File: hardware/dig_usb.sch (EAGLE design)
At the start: 180 parts, among them IC101 AT90USB1287-AU, IC102 74HC166D, IC103 MAX487CSA, IC202 DS1337S, IC301 LTV-356T, IC302 LTV-356T, IC303 LTV-356T, IC304 LTV-356T, IC305 LTV-356T, IC306 LTV-356T, IC307 LTV-356T, IC308 LTV-356T, K401 S202S02, K402 S202S02, K403 S202S02, K404 S202S02, K405 S202S02, K406 S202S02, K407 S202S02, K408 S202S02, Q1 16MHz, Q201 32,768kHz, T301 BCR191, T302 BCR191, T303 BCR191, T304 BCR191, T305 BCR191, T306 BCR191, T307 BCR191, T308 BCR191, X1 AKL_249-08, X102 ISP, X2 AKL_249-08, X3 AKL_230-02, X301 RIA-73-02, X302 RIA-73-02, X303 RIA-73-02, X304 RIA-73-02, X305 RIA-73-02, X4 AKL_230-02, X401 RIA-73-02, X402 RIA-73-02, X403 RIA-73-02, X404 RIA-73-02, X405 RIA-73-02, X406 RIA-73-02, X407 RIA-73-02, X5 AKL_230-04

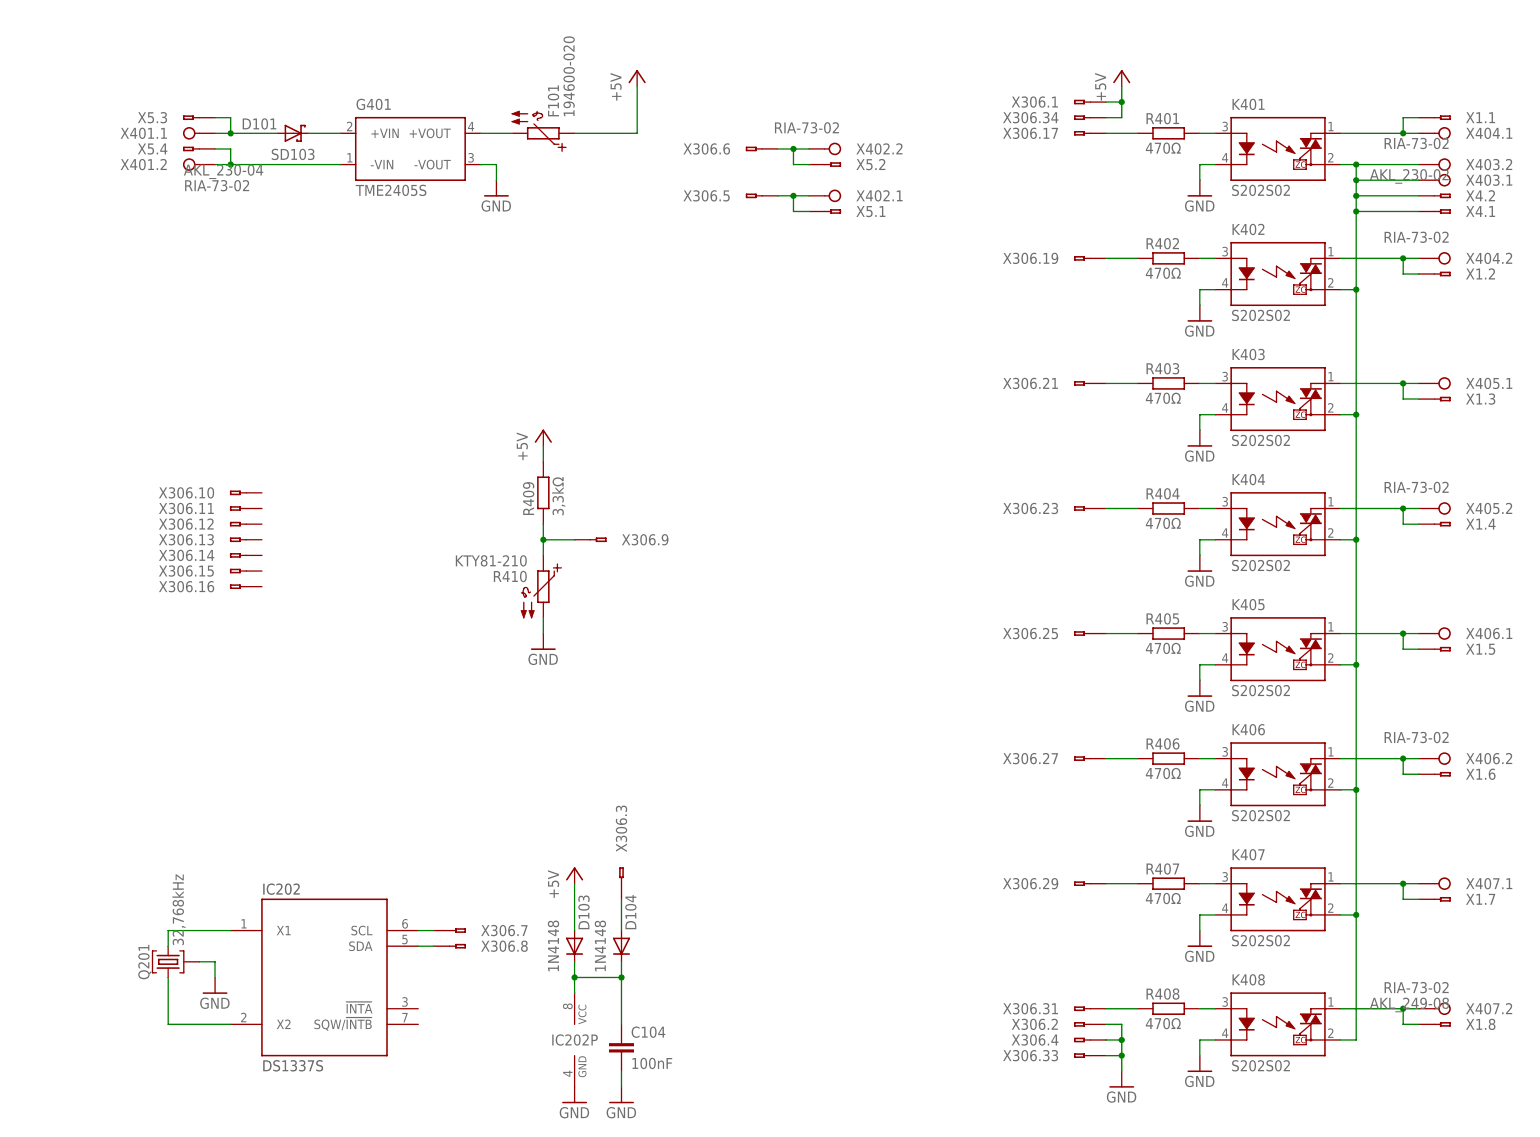
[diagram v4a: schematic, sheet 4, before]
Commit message: RJ45 Buchsen für Bus an dig_usb
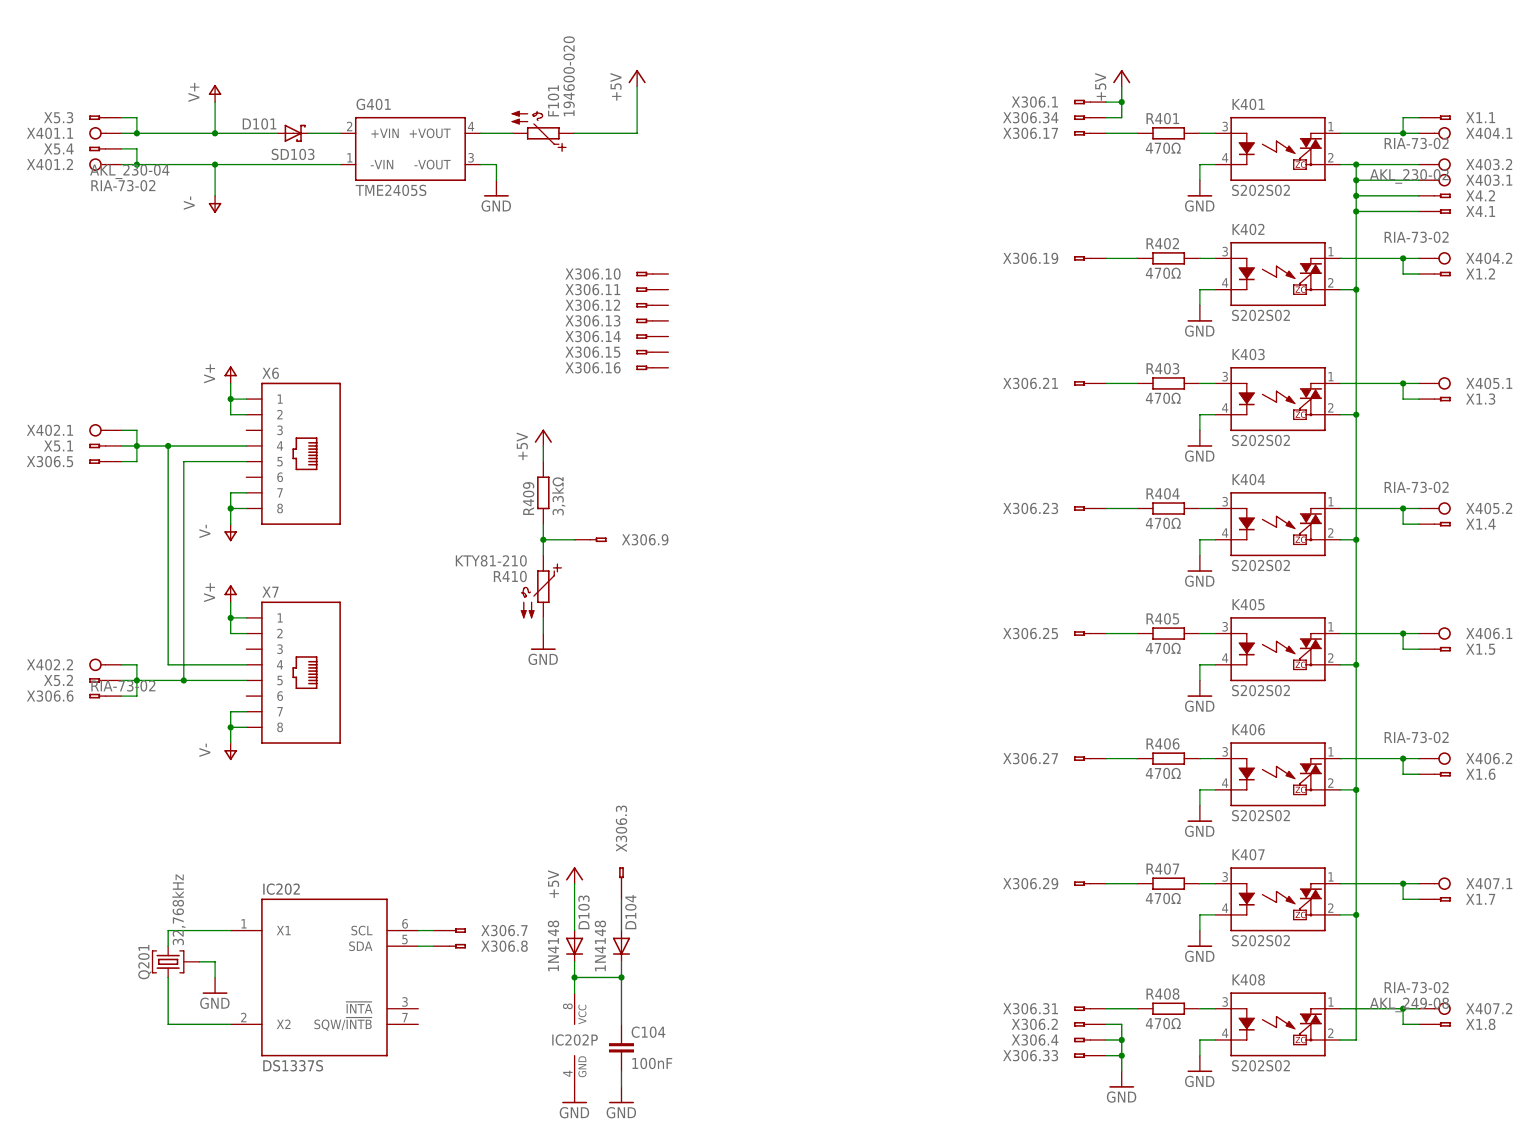
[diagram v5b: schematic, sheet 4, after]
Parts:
- added X6, X7: (no value), stecker:8P8C
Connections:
- removed net N$19: G401.-VIN, X401.2.A, X5.4.A
- removed net N$24: D101.A, X401.1.A, X5.3.A
- new net V+: D101.A, X401.1.A, X5.3.A, X6.1, X6.2, X7.1, X7.2
- new net V-: G401.-VIN, X401.2.A, X5.4.A, X6.7, X6.8, X7.7, X7.8
- net N$133: now also X6.5, X7.5
- net N$134: now also X6.4, X7.4
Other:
- moved on the sheet: X306.10, X306.11, X306.12, X306.13, X306.14, X306.15, X306.16, X306.5, X306.6, X401.1, X401.2, X402.1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

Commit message: dig_usb: Bauteile neu nummeriert und Plan etwas verschönert
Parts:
- removed C1, C2, C3, C4, C5, C6, C7, C8: 1μF, passiv:C_1206
- removed C11: 100nF, passiv:C_0805
- removed C201, C202: 100nF, passiv:C_0603
- removed D1, D11, D13, D15, D3, D5, D7, D9: 91V, diode:Z-DIODE-SOD123
- removed D10, D12, D14, D16, D2, D4, D6, D8: (no value), diode:DIODE-DO214AC
- removed D103, D104: 1N4148, diode:DIODE-SOD123
- removed D17, D18, D19, D20, D21, D22, D23, D24, D25, D26, D27, D28: GN, led:LED_0805
- removed D33: MMSZ5222BT1, diode:Z-DIODE-SOD123
- removed Q201: 32,768kHz, passiv:QM_MS1V-T1K
- removed R12, R13, R14, R15, R16, R17, R18, R19, R20, R21, R22, R23, R24, R3, R6, R9: 47kΩ, passiv:R_1206
- removed R25, R26, R27, R28, R33, R34, R35, R36, R37, R38, R39, R40: 1,5kΩ, passiv:R_0805
- removed R30: 22Ω, passiv:R_0805
- removed S2: (no value), schalter:JUMPER
- removed T301, T302, T303, T304, T305, T306, T307, T308: BCR191, transistor:PNP2R-SOT23-BEC
- removed X1, X2: AKL_249-08, anschluss:AKL_249-08
- removed X3: AKL_230-02, anschluss:AKL_230-02
- removed X5: AKL_230-04, anschluss:AKL_230-04
- removed X6, X7: (no value), stecker:8P8C
- added C110, C111, C401: 100nF, passiv:C_0603
- added C301, C302, C303, C304, C305, C306, C307, C308: 1μF, passiv:C_1206
- added D301, D303, D305, D307, D309, D311, D313, D315: MRA4007, diode:DIODE-DO214AC
- added D302, D304, D306, D308, D310, D312, D314, D316: 91V, diode:Z-DIODE-SOD123
- added D401: SD103, diode:SHOTKY-DIODE-SOD123
- added D402, D403: 1N4148, diode:DIODE-SOD123
- added LED201, LED202, LED203, LED204, LED205, LED206, LED207, LED208, LED209, LED210, LED211, LED212: GN, led:LED_0805
- added Q301, Q302, Q303, Q304, Q305, Q306, Q307, Q308: BCR191, transistor:PNP2R-SOT23-BEC
- added Q401: 32,768kHz, passiv:QM_MS1V-T1K
- added R103: 10k, passiv:R_0805
- added R106: 1MΩ, passiv:R_0805
- added R107, R108: 22kΩ, widerstandsnetzwerk:EXB-38V
- added R112: 120Ω, passiv:R_0805
- added R202, R203, R204, R205, R206, R210, R211, R212: 1,5kΩ, passiv:R_0805
- added R303, R304, R305, R306, R309, R310, R311, R312, R315, R316, R317, R318, R321, R322, R323, R324: 47kΩ, passiv:R_1206
- added S103: (no value), schalter:DP08D
- added X307, X408, X410, X411, X412: RIA-73-02, anschluss:RIA-73-02
- added X308: AKL_249-08, anschluss:AKL_249-08
- C102: device passiv:C_0603 -> passiv:C_0805
- D101: value SD103 -> MMSZ5222BT1; device diode:SHOTKY-DIODE-SOD123 -> diode:Z-DIODE-SOD123
- IC102: value 74HC166D -> MAX487CSA; device ic-logik:74HC166D -> ic-wandler:MAX487CSA
- IC103: value MAX487CSA -> 74HC166D; device ic-wandler:MAX487CSA -> ic-logik:74HC166D
- R102: value 1MΩ -> 22Ω
- R201: value 10k -> 1,5kΩ
- R207: value 120Ω -> 1,5kΩ
- R208, R209: value 22kΩ -> 1,5kΩ; device widerstandsnetzwerk:EXB-38V -> passiv:R_0805
- R401: value 470Ω -> 3,3kΩ
- R402: value 470Ω -> KTY81-210; device passiv:R_0805 -> sensor:KTY81-210
- R409: value 3,3kΩ -> 470Ω
- R410: value KTY81-210 -> 470Ω; device sensor:KTY81-210 -> passiv:R_0805
- S101: device schalter:DP08D -> schalter:JUMPER
- X301: value RIA-73-02 -> AKL_230-02; device anschluss:RIA-73-02 -> anschluss:AKL_230-02
- X303: value RIA-73-02 -> (none); device anschluss:RIA-73-02 -> anschluss:WS34V
- X306: value (none) -> RIA-73-02; device anschluss:WS34V -> anschluss:RIA-73-02
- X403: value RIA-73-02 -> AKL_230-04; device anschluss:RIA-73-02 -> anschluss:AKL_230-04
- X404, X405: value RIA-73-02 -> (none); device anschluss:RIA-73-02 -> stecker:8P8C
- X406: value RIA-73-02 -> AKL_249-08; device anschluss:RIA-73-02 -> anschluss:AKL_249-08
- renumbered C10 to C106, C12 to C103, C13 to C108, C204 to C105, C205 to C107, C9 to C109, D102 to LED104, D201 to LED101, D202 to LED102, D203 to LED103, D29 to LED213, D30 to LED214, D31 to LED215, D32 to LED216, F101 to F401, G401 to V401, IC202 to IC401, Q1 to Q101, R1 to R302, R10 to R320, R11 to R319, R2 to R301, R29 to R110, R31 to R101, R32 to R105, R4 to R308, R41 to R213, R42 to R214, R43 to R215, R44 to R216, R45 to R109, R46 to R111, R47 to R113, R48 to R104, R5 to R307, R7 to R314, R8 to R313, S1 to S102, X4 to X409
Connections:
- net !R: now also IC103A.!CLR; no longer IC102A.!CLR
- net !RESET: now also R103.1; no longer R201.1
- net +5V: now also C104.1, C110.1, C111.1, D402.A, Q301.E, Q302.E, Q303.E, Q304.E, Q305.E, Q306.E, Q307.E, Q308.E, R103.2, R401.2, S101.P$1, S103A.3, S103B.3, S103C.3, S103D.3, S103E.3, S103F.3, S103G.3, X303.1.A, X303.34.A; no longer C102.1, C201.1, C202.1, D103.A, R201.2, R409.2, S101A.3, S101B.3, S101C.3, S101D.3, S101E.3, S101F.3, S101G.3, S2.P$1, T301.E, T302.E, T303.E, T304.E, T305.E, T306.E, T307.E, T308.E, X306.1.A, X306.34.A
- net C1: now also IC103A.CK; no longer IC102A.CK
- net C2: now also IC103A.SH/!LD; no longer IC102A.SH/!LD
- net DI: now also IC103A.QH; no longer IC102A.QH
- net GND: now also C110.2, C111.2, C401.2, D101.A, IC103A.CKI, IC103A.H, IC103A.SI, Q401.G, R107.1, R107.3, R107.5, R107.7, R108.1, R108.3, R108.5, R108.7, R201.1, R202.1, R203.1, R204.1, R205.1, R206.1, R207.1, R210.1, R211.1, R212.1, R402.2, X303.2.A, X303.33.A, X303.4.A; no longer C11.2, C201.2, C202.2, D33.A, IC102A.CKI, IC102A.H, IC102A.SI, Q201.G, R208.3, R208.5, R208.7, R209.3, R209.5, R209.7, R25.1, R26.1, R27.1, R28.1, R33.1, R34.1, R35.1, R36.1, R37.1, R38.1, R39.1, R40.1, R410.2, X306.2.A, X306.33.A, X306.4.A
- net GNDIO: now also C301.2, C302.2, C303.2, C304.2, C305.2, C306.2, C307.2, C308.2, D302.A, D304.A, D306.A, D308.A, D310.A, D312.A, D314.A, D316.A, X302.1.A, X302.2.A; no longer C1.2, C2.2, C3.2, C4.2, C5.2, C6.2, C7.2, C8.2, D1.A, D11.A, D13.A, D15.A, D3.A, D5.A, D7.A, D9.A, X3.1.A, X3.2.A
- net IN0: now also LED201.A; no longer D17.A
- net IN1: now also LED202.A; no longer D18.A
- net IN2: now also LED203.A; no longer D19.A
- net IN3: now also LED204.A; no longer D20.A
- net IN4: now also LED205.A; no longer D21.A
- net IN5: now also LED206.A; no longer D22.A
- net IN6: now also LED207.A; no longer D23.A
- net IN7: now also LED208.A; no longer D24.A
- net L: now also X408.1.A, X408.2.A; no longer X403.1.A, X403.2.A
- net N$10: now also D309.A; no longer D6.A
- net N$100: now also Q306.C, X303.30.A; no longer T307.C, X306.30.A
- net N$101: now also Q308.C, X303.32.A; no longer T308.C, X306.32.A
- net N$102: now also LED201.C, R201.2; no longer D17.C, R25.2
- net N$103: now also LED202.C, R202.2; no longer D18.C, R33.2
- net N$104: now also LED203.C, R203.2; no longer D19.C, R34.2
- net N$105: now also LED204.C, R204.2; no longer D20.C, R35.2
- net N$106: now also LED205.C, R205.2; no longer D21.C, R26.2
- net N$107: now also LED206.C, R206.2; no longer D22.C, R27.2
- net N$108: now also LED207.C, R207.2; no longer D23.C, R28.2
- net N$109: now also LED208.C, R208.2; no longer D24.C, R36.2
- net N$11: now also C305.1, D309.K, D310.K, R317.2; no longer C3.1, D5.K, D6.K, R9.2
- net N$110: now also LED209.C, R209.2; no longer D25.C, R37.2
- net N$111: now also LED210.C, R210.2; no longer D26.C, R38.2
- net N$112: now also LED211.C, R211.2; no longer D27.C, R39.2
- net N$113: now also LED212.C, R212.2; no longer D28.C, R40.2
- net N$119: now also R102.1; no longer R30.1
- net N$120: now also R102.2; no longer R30.2
- net N$124: now also S101.P$2; no longer S2.P$2
- net N$126: now also Q401.2; no longer Q201.2
- net N$127: now also Q401.1; no longer Q201.1
- net N$129: now also D101.K; no longer D33.K
- net N$13: now also IC305.A, R317.1; no longer IC303.A, R9.1
- net N$130: now also D403.A, X303.3.A; no longer D104.A, X306.3.A
- net N$131: now also X303.7.A; no longer X306.7.A
- net N$132: now also X303.8.A; no longer X306.8.A
- net N$133: now also X303.6.A, X403.2.A, X404.5, X405.5; no longer X306.6.A, X5.2.A, X6.5, X7.5
- net N$134: now also X303.5.A, X403.1.A, X404.4, X405.4; no longer X306.5.A, X5.1.A, X6.4, X7.4
- net N$14: now also D313.A; no longer D8.A
- net N$143: now also R106.1; no longer R102.1
- net N$146: now also R401.1, R402.1, X303.9.A; no longer R409.1, R410.1, X306.9.A
- net N$15: now also C307.1, D313.K, D314.K, R323.2; no longer C4.1, D7.K, D8.K, R12.2
- net N$16: now also R404.2; no longer R402.2
- net N$2: now also D301.A; no longer D2.A
- net N$20: now also IC102A.A, S103H.4; no longer IC103A.A, S101H.4
- net N$21: now also R106.2; no longer R102.2
- net N$22: now also IC102A.B, R112.1; no longer IC103A.B, R207.1
- net N$23: now also D401.K; no longer D101.K
- net N$25: now also R405.2; no longer R403.2
- net N$26: now also IC103A.A, R107.2, S103A.4; no longer IC102A.A, R208.2, S101A.4
- net N$27: now also IC103A.B, R107.4, S103B.4; no longer IC102A.B, R208.4, S101B.4
- net N$28: now also IC103A.C, R107.6, S103C.4; no longer IC102A.C, R208.6, S101C.4
- net N$29: now also IC103A.D, R107.8, S103D.4; no longer IC102A.D, R208.8, S101D.4
- net N$3: now also C301.1, D301.K, D302.K, R305.2; no longer C1.1, D1.K, D2.K, R3.2
- net N$30: now also IC103A.E, R108.2, S103E.4; no longer IC102A.E, R209.2, S101E.4
- net N$31: now also IC103A.F, R108.4, S103F.4; no longer IC102A.F, R209.4, S101F.4
- net N$32: now also IC103A.G, R108.6, S103G.4; no longer IC102A.G, R209.6, S101G.4
- net N$33: now also R112.2, S103H.3; no longer R207.2, S101H.3
- net N$34: now also IC307.A, R323.1; no longer IC304.A, R12.1
- net N$35: now also D303.A, R304.1; no longer D10.A, R13.1
- net N$36: now also C302.1, D303.K, D304.K, R306.2; no longer C5.1, D10.K, D9.K, R15.2
- net N$37: now also R406.2; no longer R404.2
- net N$38: now also IC302.A, R306.1; no longer IC305.A, R15.1
- net N$39: now also D307.A, R310.1; no longer D12.A, R16.1
- net N$40: now also C304.1, D307.K, D308.K, R312.2; no longer C6.1, D11.K, D12.K, R18.2
- net N$42: now also R407.2; no longer R405.2
- net N$45: now also X304.1.A, X308.7.A; no longer X2.7.A, X302.1.A
- net N$46: now also X304.2.A, X308.8.A; no longer X2.8.A, X302.2.A
- net N$47: now also X306.1.A, X308.5.A; no longer X2.5.A, X303.1.A
- net N$48: now also X306.2.A, X308.6.A; no longer X2.6.A, X303.2.A
- net N$49: now also R303.1, R304.2; no longer R13.2, R14.1
- net N$5: now also R305.1; no longer R3.1
- net N$50: now also R408.2; no longer R406.2
- net N$51: now also R309.1, R310.2; no longer R16.2, R17.1
- net N$52: now also IC307.C, Q307.B; no longer IC304.C, T304.B
- net N$53: now also R315.1, R316.2; no longer R19.2, R20.1
- net N$54: now also R321.1, R322.2; no longer R22.2, R23.1
- net N$55: now also IC304.A, R312.1; no longer IC306.A, R18.1
- net N$56: now also R303.2, X305.2.A, X308.4.A; no longer R14.2, X2.4.A, X304.2.A
- net N$57: now also D311.A, R316.1; no longer D14.A, R19.1
- net N$58: now also R309.2, X305.1.A, X308.3.A; no longer R17.2, X2.3.A, X304.1.A
- net N$59: now also R321.2, X307.1.A, X308.1.A; no longer R23.2, X2.1.A, X305.1.A
- net N$6: now also D305.A; no longer D4.A
- net N$60: now also R315.2, X307.2.A, X308.2.A; no longer R20.2, X2.2.A, X305.2.A
- net N$61: now also R409.2; no longer R407.2
- net N$64: now also C401.1, D402.K, D403.K; no longer C104.1, D103.K, D104.K
- net N$65: now also C306.1, D311.K, D312.K, R318.2; no longer C7.1, D13.K, D14.K, R21.2
- net N$66: now also R410.2; no longer R408.2
- net N$67: now also R403.1, X303.17.A; no longer R401.1, X306.17.A
- net N$68: now also X406.1.A, X407.1.A; no longer X1.1.A, X404.1.A
- net N$69: now also IC306.A, R318.1; no longer IC307.A, R21.1
- net N$7: now also C303.1, D305.K, D306.K, R311.2; no longer C2.1, D3.K, D4.K, R6.2
- net N$70: now also IC305.C, Q305.B; no longer IC303.C, T303.B
- net N$71: now also D315.A, R322.1; no longer D16.A, R22.1
- net N$72: now also X406.2.A, X407.2.A; no longer X1.2.A, X404.2.A
- net N$73: now also IC303.C, Q303.B; no longer IC302.C, T302.B
- net N$74: now also X406.3.A, X410.1.A; no longer X1.3.A, X405.1.A
- net N$75: now also Q301.B; no longer T301.B
- net N$76: now also X406.4.A, X410.2.A; no longer X1.4.A, X405.2.A
- net N$77: now also C308.1, D315.K, D316.K, R324.2; no longer C8.1, D15.K, D16.K, R24.2
- net N$78: now also X406.5.A, X411.1.A; no longer X1.5.A, X406.1.A
- net N$79: now also R404.1, X303.19.A; no longer R402.1, X306.19.A
- net N$8: now also R403.2; no longer R401.2
- net N$80: now also IC302.C, Q302.B; no longer IC305.C, T305.B
- net N$81: now also IC304.C, Q304.B; no longer IC306.C, T306.B
- net N$82: now also X406.6.A, X411.2.A; no longer X1.6.A, X406.2.A
- net N$83: now also IC306.C, Q306.B; no longer IC307.C, T307.B
- net N$84: now also X406.7.A, X412.1.A; no longer X1.7.A, X407.1.A
- net N$85: now also Q308.B; no longer T308.B
- net N$86: now also R324.1; no longer R24.1
- net N$87: now also R405.1, X303.21.A; no longer R403.1, X306.21.A
- net N$88: now also R406.1, X303.23.A; no longer R404.1, X306.23.A
- net N$89: now also X406.8.A, X412.2.A; no longer X1.8.A, X407.2.A
- net N$9: now also IC303.A, R311.1; no longer IC302.A, R6.1
- net N$90: now also R407.1, X303.25.A; no longer R405.1, X306.25.A
- net N$91: now also R408.1, X303.27.A; no longer R406.1, X306.27.A
- net N$92: now also R409.1, X303.29.A; no longer R407.1, X306.29.A
- net N$93: now also R410.1, X303.31.A; no longer R408.1, X306.31.A
- net N$94: now also Q301.C, X303.18.A; no longer T301.C, X306.18.A
- net N$95: now also Q303.C, X303.20.A; no longer T302.C, X306.20.A
- net N$96: now also Q305.C, X303.22.A; no longer T303.C, X306.22.A
- net N$97: now also Q307.C, X303.24.A; no longer T304.C, X306.24.A
- net N$98: now also Q302.C, X303.26.A; no longer T305.C, X306.26.A
- net N$99: now also Q304.C, X303.28.A; no longer T306.C, X306.28.A
- net OUT0: now also LED209.A; no longer D25.A
- net OUT1: now also LED210.A; no longer D26.A
- net OUT2: now also LED211.A; no longer D27.A
- net OUT3: now also LED212.A; no longer D28.A
- net RE: now also IC102A.RE/; no longer IC103A.RE/
- net RXD: now also IC102A.RO; no longer IC103A.RO
- net TE: now also IC102A.DE; no longer IC103A.DE
- net TXD: now also IC102A.DI; no longer IC103A.DI
- net USHIELD: now also C102.1; no longer C11.1
- net V+: now also D401.A, X403.3.A, X404.1, X404.2, X405.1, X405.2; no longer D101.A, X5.3.A, X6.1, X6.2, X7.1, X7.2
- net V-: now also X403.4.A, X404.7, X404.8, X405.7, X405.8; no longer X5.4.A, X6.7, X6.8, X7.7, X7.8

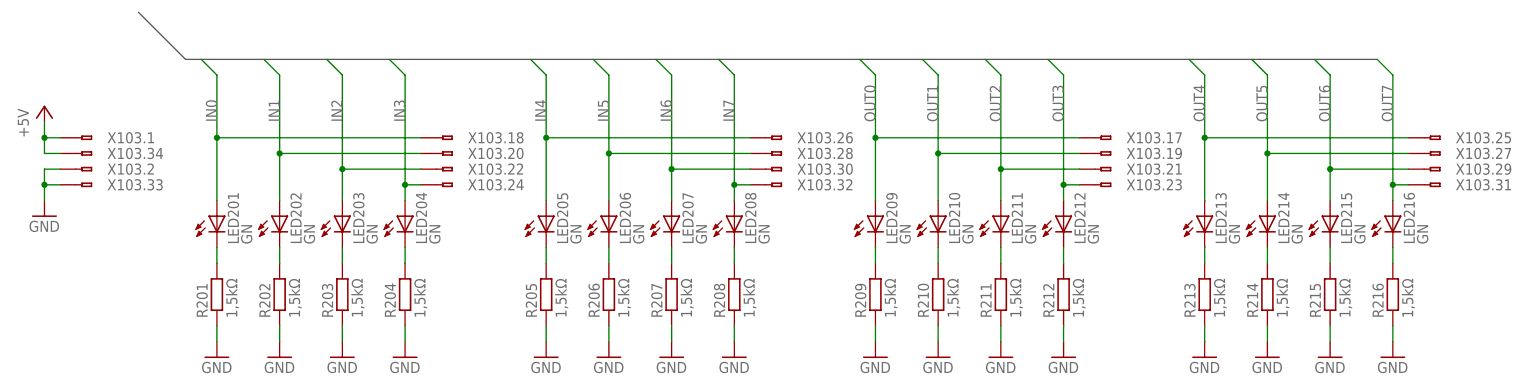
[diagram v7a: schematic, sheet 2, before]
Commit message: dig_usb: Beschriftung besser angeordnet
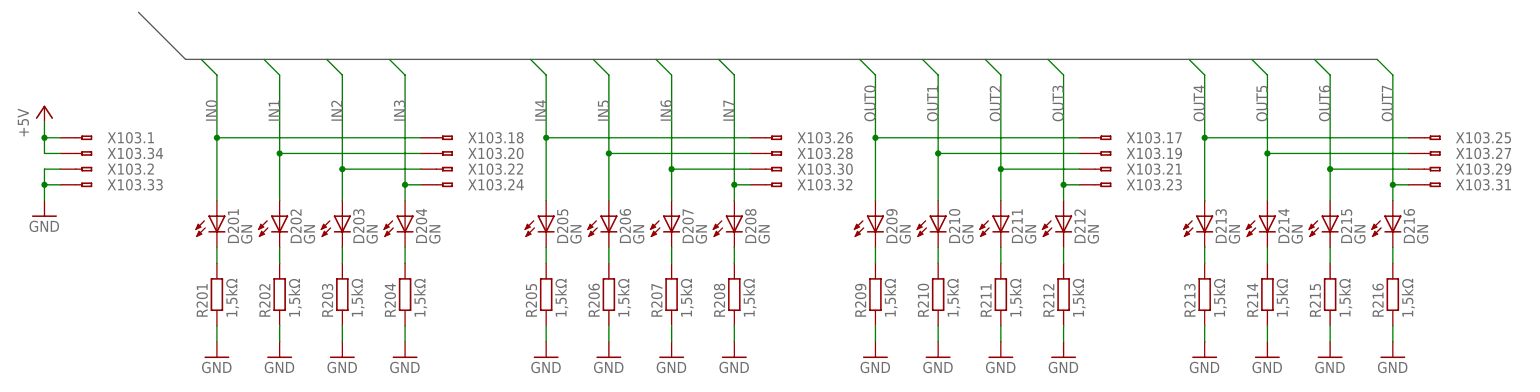
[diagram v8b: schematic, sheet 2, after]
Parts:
- X308, X406: value AKL_249-08 -> AKL_230-08; device anschluss:AKL_249-08 -> anschluss:AKL_230-08
- renumbered LED101 to D102, LED102 to D103, LED103 to D104, LED104 to D105, LED201 to D201, LED202 to D202, LED203 to D203, LED204 to D204, LED205 to D205, LED206 to D206, LED207 to D207, LED208 to D208, LED209 to D209, LED210 to D210, LED211 to D211, LED212 to D212, LED213 to D213, LED214 to D214, LED215 to D215, LED216 to D216
